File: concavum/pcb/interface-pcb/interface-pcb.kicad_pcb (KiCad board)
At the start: 2 copper layers, 29 x 38 mm, 20 parts, among them J1 USB_C_Port, J2 Audio_Jack, J3 ISP_pads, J4 FPC_connector, U1 ATmega32U4-A, U2 MCP23017_SO, Y1 Crystal_16MHz

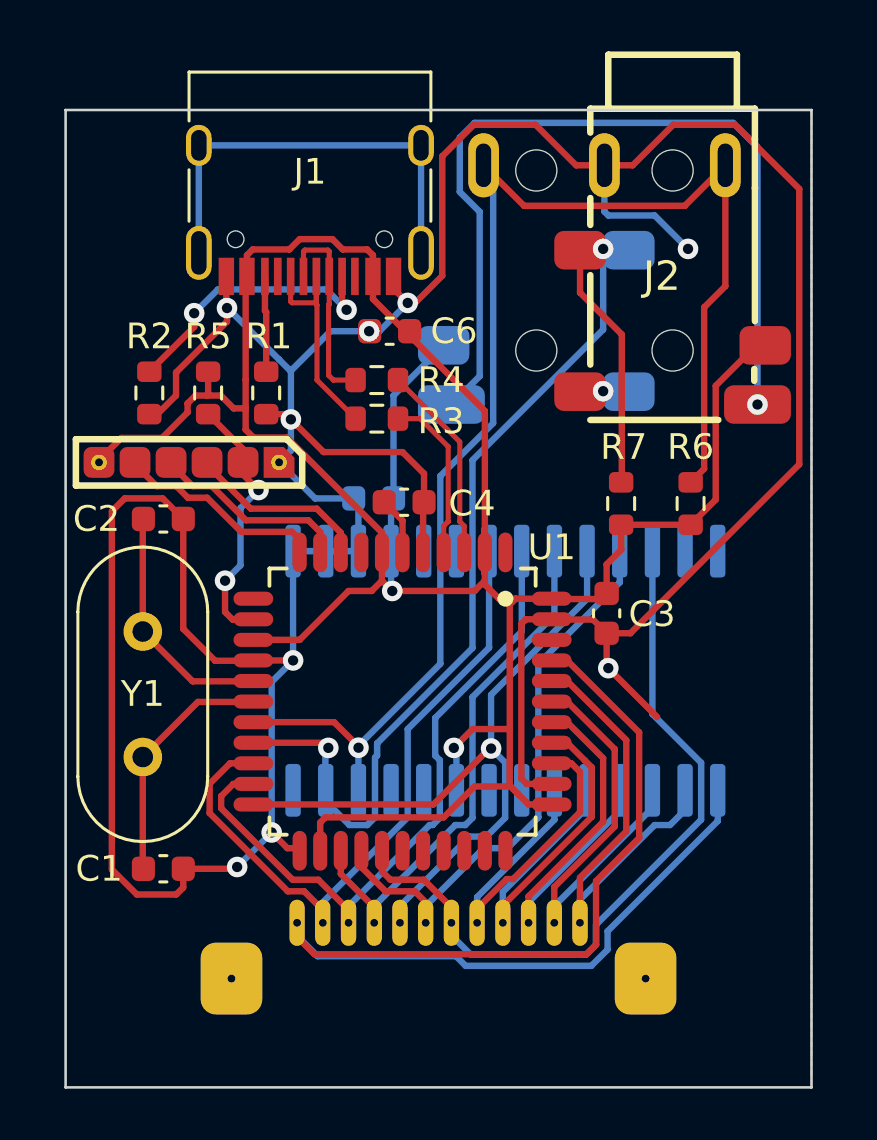
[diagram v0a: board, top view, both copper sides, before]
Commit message: Change port expander row and column pins
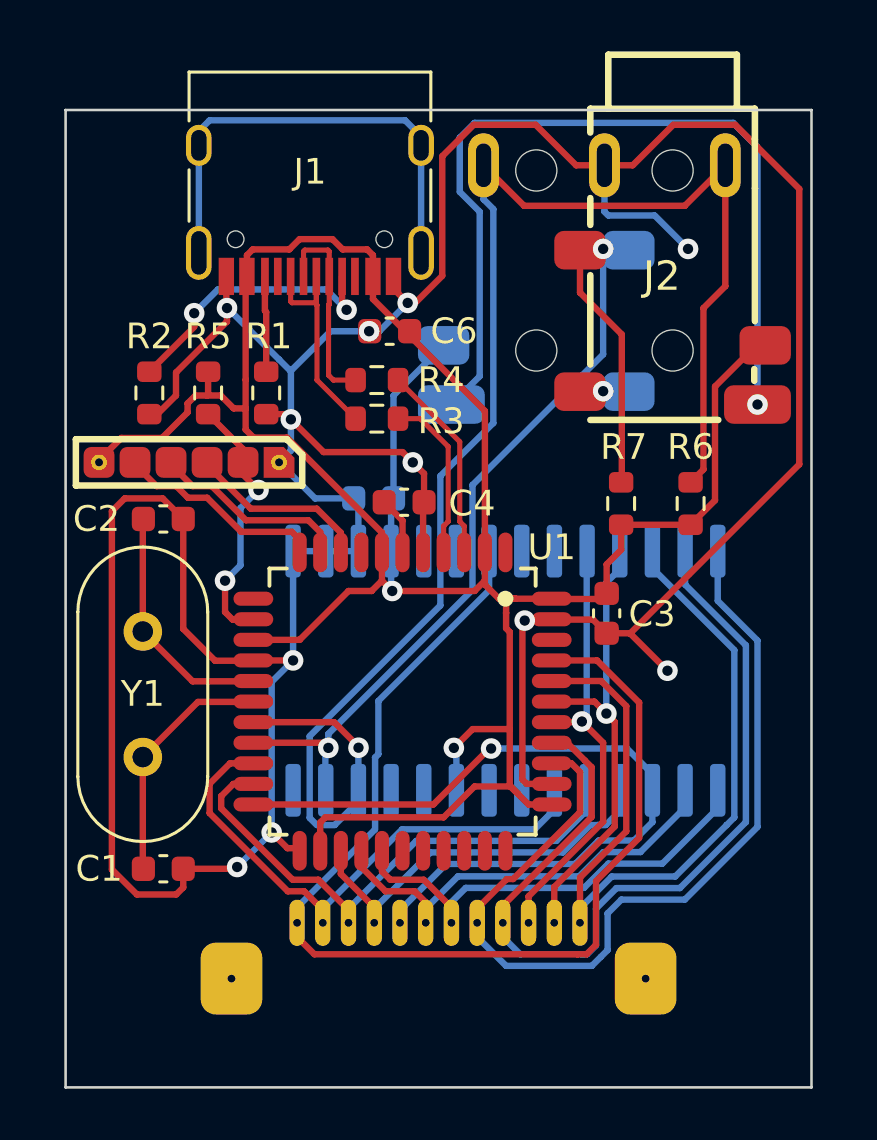
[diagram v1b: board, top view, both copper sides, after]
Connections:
- U2 pad 1: /ROW1 -> /COL6
- U2 pad 10: unconnected-(U2-Pad10) -> GND
- U2 pad 2: /ROW6 -> /COL5
- U2 pad 21: /COL1 -> /ROW1
- U2 pad 22: /COL2 -> unconnected-(U2-Pad22)
- U2 pad 23: /COL3 -> unconnected-(U2-Pad23)
- U2 pad 24: /COL4 -> /ROW4
- U2 pad 25: /COL5 -> /ROW5
- U2 pad 26: /COL6 -> /ROW6
- U2 pad 27: unconnected-(U2-Pad27) -> /ROW3
- U2 pad 28: unconnected-(U2-Pad28) -> /ROW2
- U2 pad 3: /ROW5 -> /COL4
- U2 pad 4: /ROW4 -> /COL3
- U2 pad 5: /ROW3 -> /COL2
- U2 pad 6: /ROW2 -> /COL1
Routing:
- net /ROW2: track 16.0 -> 35.9 mm
- net /ROW3: track 16.0 -> 34.3 mm
- net /ROW6: track 19.0 -> 32.3 mm
- net /COL6: track 29.6 -> 18.6 mm
- net /SCL: track 54.6 -> 61.0 mm
- net /COL2: track 26.6 -> 21.3 mm
- net /COL5: track 22.7 -> 17.5 mm
- net /COL3: track 20.8 -> 15.7 mm
- net /SDA: track 42.9 -> 38.1 mm
- net /COL1: track 26.1 -> 21.6 mm
- net /ROW1: track 47.5 -> 44.4 mm
- net GND: track 150.3 -> 148.3 mm, vias 9 -> 11
- net /COL4: track 28.3 -> 30.3 mm
- net unconnected-(J1-PadS1): track 17.0 -> 18.3 mm
- net /ROW4: track 16.9 -> 17.4 mm, vias 0 -> 1
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
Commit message: Add M2 mounting holes
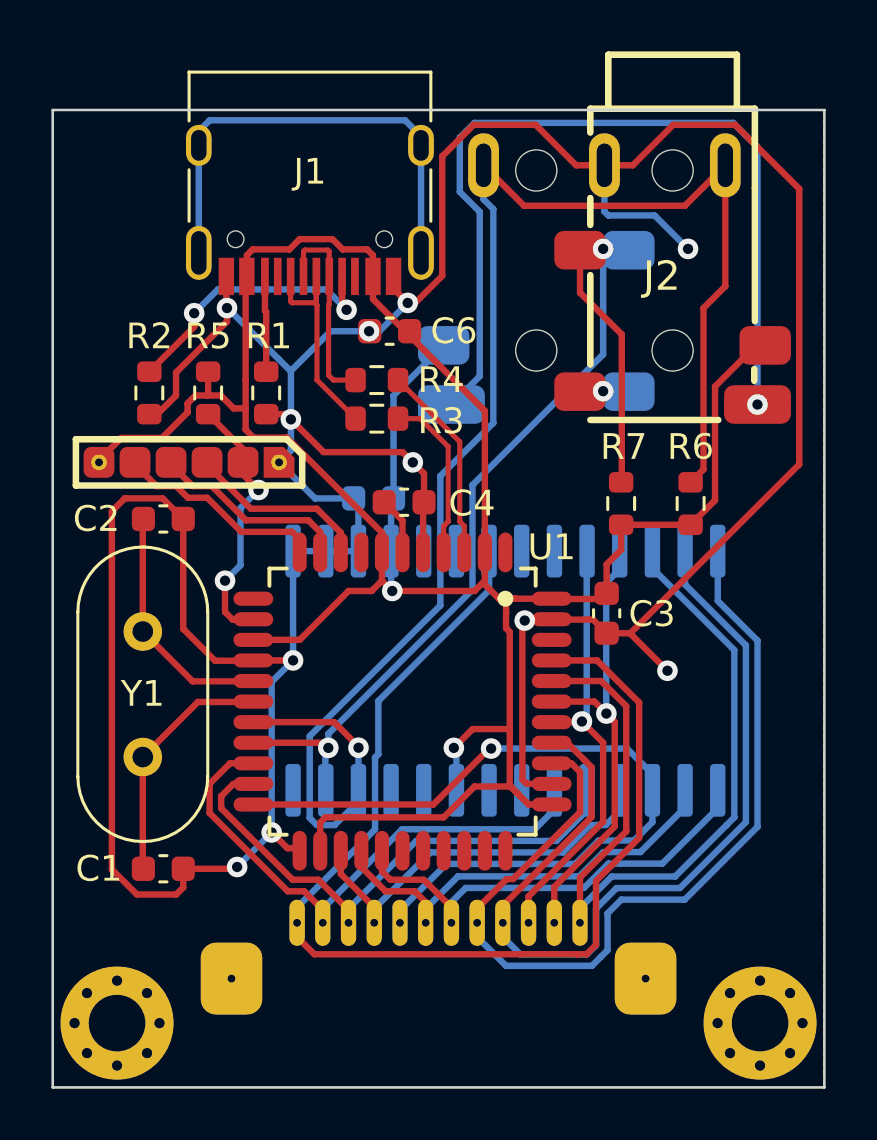
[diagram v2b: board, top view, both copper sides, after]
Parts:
- added H1: MountingHole_Pad, MountingHole:MountingHole_2.2mm_M2_Pad_Via, F.Cu at (142.0, 115.5)
- added H2: MountingHole_Pad, MountingHole:MountingHole_2.2mm_M2_Pad_Via, F.Cu at (167.0, 115.5)
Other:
- board size 29 x 38 mm -> 30 x 38 mm
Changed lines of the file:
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@@
   (net 51 "unconnected-(J1-PadB8)")
   (net 52 "unconnected-(J1-PadA8)")
+  (net 53 "unconnected-(H1-Pad1)")
+  (net 54 "unconnected-(H2-Pad1)")
   (footprint "Capacitor_SMD:C_0603_1608Metric" (layer "F.Cu")
     (at 152.6 88.6 180)
@@
       (rotate (xyz 0 0 0))
     )
+  )
+  (footprint "MountingHole:MountingHole_2.2mm_M2_Pad_Via" (layer "F.Cu")
+    (at 167 115.5)
+    (descr "Mounting Hole 2.2mm, M2")
+    (tags "mounting hole 2.2mm m2")
+    (property "Sheetfile" "interface-pcb.kicad_sch")
+    (property "Sheetname" "")
+    (attr exclude_from_pos_files)
+    (fp_text reference "H2" (at 0 -3.2) (layer "F.SilkS") hide
+      (effects (font (size 1 1) (thickness 0.15)))
+    )
+    (fp_text value "MountingHole_Pad" (at 0 3.2) (layer "F.Fab")
+      (effects (font (size 1 1) (thickness 0.15)))
+    )
+    (fp_text user "${REFERENCE}" (at 0.3 0) (layer "F.Fab")
+      (effects (font (size 1 1) (thickness 0.15)))
+    )
+    (fp_circle (center 0 0) (end 2.2 0) (layer "Cmts.User") (width 0.15) (fill none))
+    (fp_circle (center 0 0) (end 2.45 0) (layer "F.CrtYd") (width 0.05) (fill none))
+    (pad "1" thru_hole circle (at 1.166726 1.166726) (size 0.7 0.7) (drill 0.4) (layers *.Cu *.Mask)
+      (net 54 "unconnected-(H2-Pad1)") (pinfunction "1") (pintype "input+no_connect"))
+    (pad "1" thru_hole circle (at 0 0) (size 4.4 4.4) (drill 2.2) (layers *.Cu *.Mask)
+      (net 54 "unconnected-(H2-Pad1)") (pinfunction "1") (pintype "input+no_connect"))
+    (pad "1" thru_hole circle (at 0 1.65) (size 0.7 0.7) (drill 0.4) (layers *.Cu *.Mask)
+      (net 54 "unconnected-(H2-Pad1)") (pinfunction "1") (pintype "input+no_connect"))
+    (pad "1" thru_hole circle (at 1.166726 -1.166726) (size 0.7 0.7) (drill 0.4) (layers *.Cu *.Mask)
+      (net 54 "unconnected-(H2-Pad1)") (pinfunction "1") (pintype "input+no_connect"))
+    (pad "1" thru_hole circle (at -1.166726 -1.166726) (size 0.7 0.7) (drill 0.4) (layers *.Cu *.Mask)
+      (net 54 "unconnected-(H2-Pad1)") (pinfunction "1") (pintype "input+no_connect"))
+    (pad "1" thru_hole circle (at 1.65 0) (size 0.7 0.7) (drill 0.4) (layers *.Cu *.Mask)
+      (net 54 "unconnected-(H2-Pad1)") (pinfunction "1") (pintype "input+no_connect"))
+    (pad "1" thru_hole circle (at 0 -1.65) (size 0.7 0.7) (drill 0.4) (layers *.Cu *.Mask)
+      (net 54 "unconnected-(H2-Pad1)") (pinfunction "1") (pintype "input+no_connect"))
+    (pad "1" thru_hole circle (at -1.65 0) (size 0.7 0.7) (drill 0.4) (layers *.Cu *.Mask)
+      (net 54 "unconnected-(H2-Pad1)") (pinfunction "1") (pintype "input+no_connect"))
+    (pad "1" thru_hole circle (at -1.166726 1.166726) (size 0.7 0.7) (drill 0.4) (layers *.Cu *.Mask)
+      (net 54 "unconnected-(H2-Pad1)") (pinfunction "1") (pintype "input+no_connect"))
   )
   (footprint "Resistor_SMD:R_0603_1608Metric" (layer "F.Cu")
@@
       (rotate (xyz 0 0 0))
     )
+  )
+  (footprint "MountingHole:MountingHole_2.2mm_M2_Pad_Via" (layer "F.Cu")
+    (at 142 115.5)
+    (descr "Mounting Hole 2.2mm, M2")
+    (tags "mounting hole 2.2mm m2")
+    (property "Sheetfile" "interface-pcb.kicad_sch")
+    (property "Sheetname" "")
+    (attr exclude_from_pos_files)
+    (fp_text reference "H1" (at 0 -3.2) (layer "F.SilkS") hide
+      (effects (font (size 1 1) (thickness 0.15)))
+    )
+    (fp_text value "MountingHole_Pad" (at 0 3.5) (layer "F.Fab")
+      (effects (font (size 1 1) (thickness 0.15)))
+    )
+    (fp_text user "${REFERENCE}" (at 0.3 0) (layer "F.Fab")
+      (effects (font (size 1 1) (thickness 0.15)))
+    )
+    (fp_circle (center 0 0) (end 2.2 0) (layer "Cmts.User") (width 0.15) (fill none))
+    (fp_circle (center 0 0) (end 2.45 0) (layer "F.CrtYd") (width 0.05) (fill none))
+    (pad "1" thru_hole circle (at -1.65 0) (size 0.7 0.7) (drill 0.4) (layers *.Cu *.Mask)
+      (net 53 "unconnected-(H1-Pad1)") (pinfunction "1") (pintype "input+no_connect"))
+    (pad "1" thru_hole circle (at 0 0) (size 4.4 4.4) (drill 2.2) (layers *.Cu *.Mask)
+      (net 53 "unconnected-(H1-Pad1)") (pinfunction "1") (pintype "input+no_connect"))
+    (pad "1" thru_hole circle (at 1.166726 1.166726) (size 0.7 0.7) (drill 0.4) (layers *.Cu *.Mask)
+      (net 53 "unconnected-(H1-Pad1)") (pinfunction "1") (pintype "input+no_connect"))
+    (pad "1" thru_hole circle (at -1.166726 1.166726) (size 0.7 0.7) (drill 0.4) (layers *.Cu *.Mask)
+      (net 53 "unconnected-(H1-Pad1)") (pinfunction "1") (pintype "input+no_connect"))
+    (pad "1" thru_hole circle (at 0 1.65) (size 0.7 0.7) (drill 0.4) (layers *.Cu *.Mask)
+      (net 53 "unconnected-(H1-Pad1)") (pinfunction "1") (pintype "input+no_connect"))
+    (pad "1" thru_hole circle (at -1.166726 -1.166726) (size 0.7 0.7) (drill 0.4) (layers *.Cu *.Mask)
+      (net 53 "unconnected-(H1-Pad1)") (pinfunction "1") (pintype "input+no_connect"))
+    (pad "1" thru_hole circle (at 1.166726 -1.166726) (size 0.7 0.7) (drill 0.4) (layers *.Cu *.Mask)
+      (net 53 "unconnected-(H1-Pad1)") (pinfunction "1") (pintype "input+no_connect"))
+    (pad "1" thru_hole circle (at 1.65 0) (size 0.7 0.7) (drill 0.4) (layers *.Cu *.Mask)
+      (net 53 "unconnected-(H1-Pad1)") (pinfunction "1") (pintype "input+no_connect"))
+    (pad "1" thru_hole circle (at 0 -1.65) (size 0.7 0.7) (drill 0.4) (layers *.Cu *.Mask)
+      (net 53 "unconnected-(H1-Pad1)") (pinfunction "1") (pintype "input+no_connect"))
   )
   (footprint "Custom:TQFP-44-Rounded-Pads" (layer "F.Cu")
@@
     )
   )
-  (gr_line (start 140 80) (end 140 118) (layer "Edge.Cuts") (width 0.1))
-  (gr_line (start 169 80) (end 140 80) (layer "Edge.Cuts") (width 0.1))
-  (gr_line (start 140 118) (end 169 118) (layer "Edge.Cuts") (width 0.1))
-  (gr_line (start 169 118) (end 169 80) (layer "Edge.Cuts") (width 0.1))
-  (dimension (type orthogonal) (layer "Dwgs.User")
-    (pts (xy 140.2 82.4) (xy 169.2 82.4))
-    (height -8.4)
-    (orientation 0)
-    (gr_text "29,0000 mm" (at 154.7 72.85) (layer "Dwgs.User")
+  (gr_line (start 139.5 80) (end 139.5 118) (layer "Edge.Cuts") (width 0.1))
+  (gr_line (start 169.5 80) (end 139.5 80) (layer "Edge.Cuts") (width 0.1))
+  (gr_line (start 139.5 118) (end 169.5 118) (layer "Edge.Cuts") (width 0.1))
+  (gr_line (start 169.5 118) (end 169.5 80) (layer "Edge.Cuts") (width 0.1))
+  (dimension (type aligned) (layer "F.Fab")
+    (pts (xy 142 117.5) (xy 167 117.5))
+    (height 8.5)
+    (gr_text "25,0000 mm" (at 154.5 124.85) (layer "F.Fab")
       (effects (font (size 1 1) (thickness 0.15)))
     )
     (format (units 3) (units_format 1) (precision 4))
-    (style (thickness 0.15) (arrow_length 1.27) (text_position_mode 0) (extension_height 0.58642) (extension_offset 0.5) keep_text_aligned)
-  )
-  (dimension (type orthogonal) (layer "Dwgs.User")
-    (pts (xy 140.7 80) (xy 140.7 118))
-    (height -6.7)
-    (orientation 1)
-    (gr_text "38,0000 mm" (at 132.85 99 90) (layer "Dwgs.User")
+    (style (thickness 0.1) (arrow_length 1.27) (text_position_mode 0) (extension_height 0.58642) (extension_offset 0.5) keep_text_aligned)
+  )
+  (dimension (type aligned) (layer "F.Fab")
+    (pts (xy 139.5 80) (xy 139.5 118))
+    (height 4.999999)
+    (gr_text "38,0000 mm" (at 133.350001 99 90) (layer "F.Fab")
       (effects (font (size 1 1) (thickness 0.15)))
     )
     (format (units 3) (units_format 1) (precision 4))
-    (style (thickness 0.15) (arrow_length 1.27) (text_position_mode 0) (extension_height 0.58642) (extension_offset 0.5) keep_text_aligned)
+    (style (thickness 0.1) (arrow_length 1.27) (text_position_mode 0) (extension_height 0.58642) (extension_offset 0.5) keep_text_aligned)
+  )
+  (dimension (type aligned) (layer "F.Fab")
+    (pts (xy 139.5 80) (xy 169.5 80))
+    (height -5.5)
+    (gr_text "30,0000 mm" (at 154.5 73.35) (layer "F.Fab")
+      (effects (font (size 1 1) (thickness 0.15)))
+    )
+    (format (units 3) (units_format 1) (precision 4))
+    (style (thickness 0.1) (arrow_length 1.27) (text_position_mode 0) (extension_height 0.58642) (extension_offset 0.5) keep_text_aligned)
   )
   (segment (start 147.182 103) (end 147.169 103.013) (width 0.25) (layer "F.Cu") (net 1))
@@
     (polygon
       (pts
-        (xy 169 118)
-        (xy 140 118)
-        (xy 140 80)
-        (xy 169 80)
+        (xy 169.5 118)
+        (xy 139.5 118)
+        (xy 139.5 80)
+        (xy 169.5 80)
       )
     )
@@
     (polygon
       (pts
-        (xy 169 118)
-        (xy 140 118)
-        (xy 140 80)
-        (xy 169 80)
+        (xy 169.5 118)
+        (xy 139.5 118)
+        (xy 139.5 80)
+        (xy 169.5 80)
       )
     )

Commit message: Add OSHW logo and URL
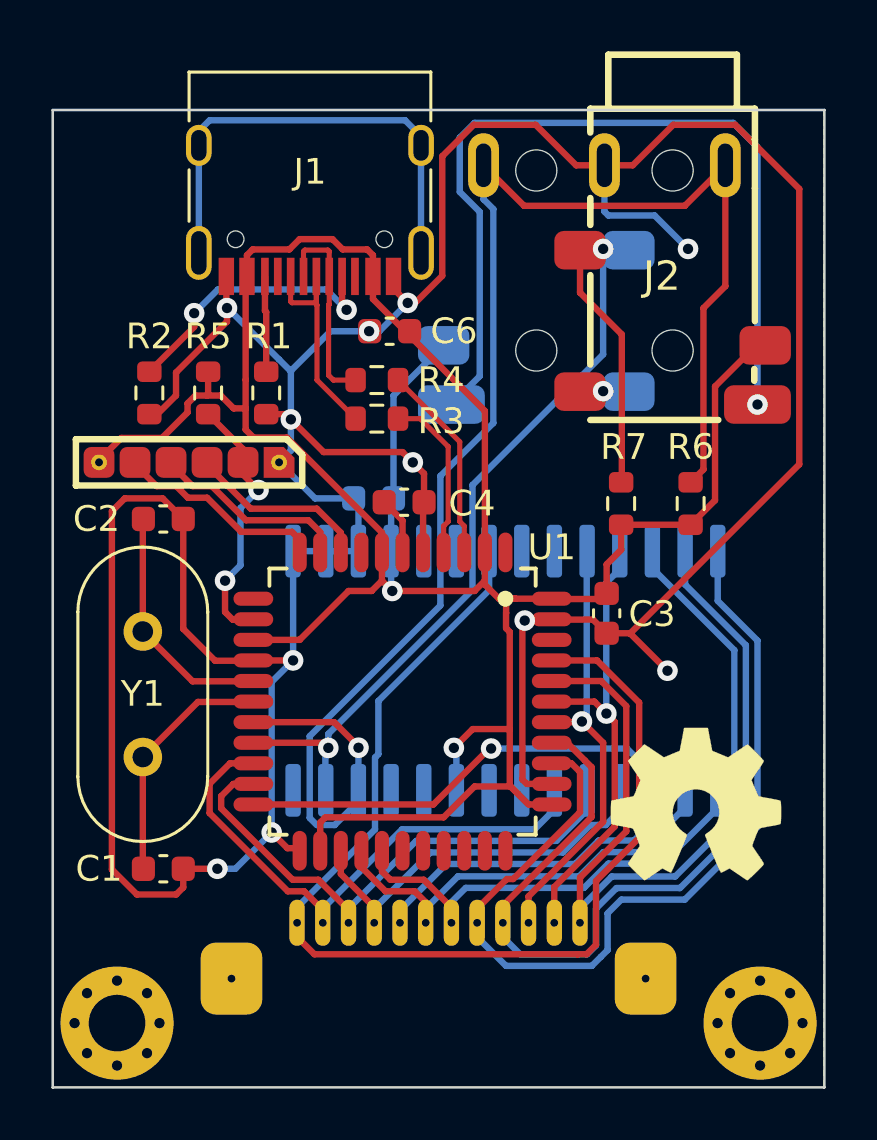
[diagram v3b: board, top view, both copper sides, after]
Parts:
- added REF**: OSHW-Symbol_6.7x6mm_SilkScreen, Symbol:OSHW-Symbol_6.7x6mm_SilkScreen, F.Cu at (164.5, 107.0)
- added REF**: OSHW-Symbol_6.7x6mm_SilkScreen, Symbol:OSHW-Symbol_6.7x6mm_SilkScreen, B.Cu at (144.5, 91.5)
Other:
- board text added: "github.com/julianschuler/keyboards"
